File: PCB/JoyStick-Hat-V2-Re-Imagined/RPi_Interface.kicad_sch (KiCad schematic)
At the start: 19 parts, among them J7 Raspberry_Pi_2_3

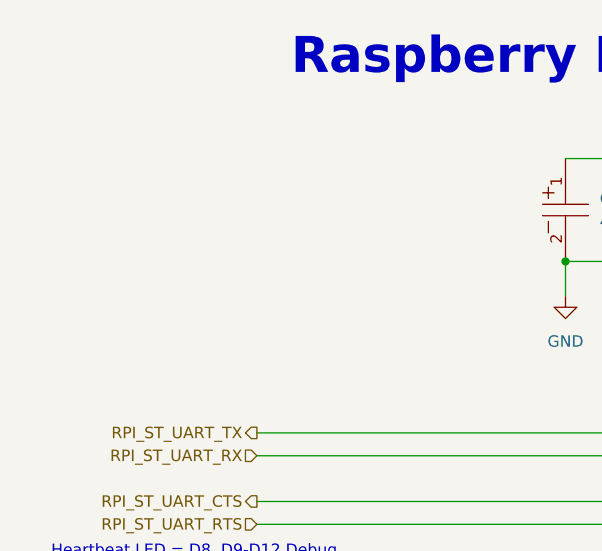
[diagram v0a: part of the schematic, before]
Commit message: V2
Lots of progress made on version two of JoyStick Hat but the RPi 5 is going to be elimintated and an additional RS485 port added.
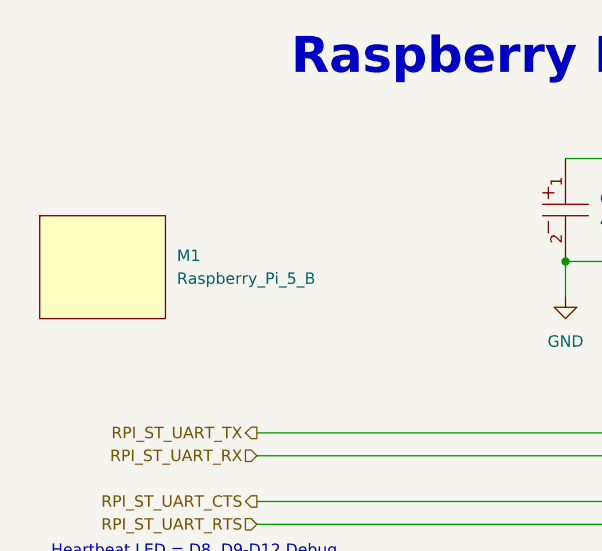
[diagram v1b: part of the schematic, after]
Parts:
- added M1: Raspberry_Pi_5_B, AVR-KiCAD-Lib-Modules:Raspberry_Pi_5, symbol AVR-KiCAD-Lib-Modules:Raspberry_Pi_5_B
